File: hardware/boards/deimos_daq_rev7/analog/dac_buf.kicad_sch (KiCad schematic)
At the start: 4 parts, among them IC53001 INA826AIDR

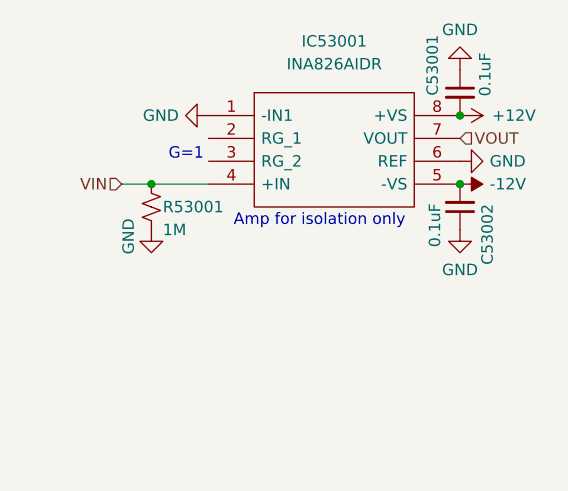
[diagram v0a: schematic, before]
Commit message: schematic updates for ovp rail and dac pulldown
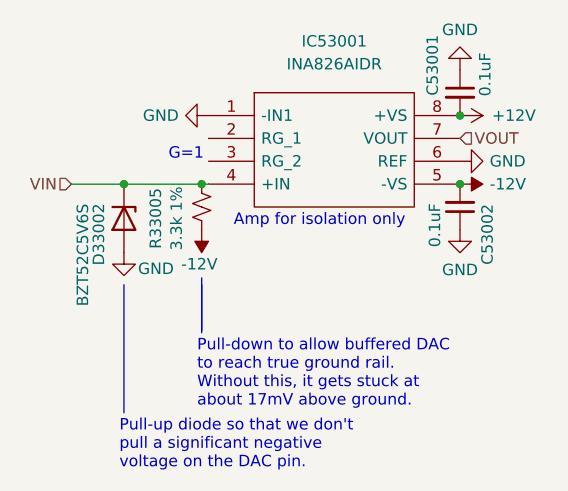
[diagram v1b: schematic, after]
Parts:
- removed R53001: 1M, Resistor_SMD:R_0402_1005Metric, symbol Device:R_Small_US
- added D33002: BZT52C5V6S, Diode_SMD:D_SOD-323, symbol Device:D_Zener
- added R33005: 3.3k 1%, Resistor_SMD:R_0402_1005Metric, symbol Device:R_Small_US
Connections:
- net -12V: now also R33005.1
- net GND: now also D33002.2 (A)
- net VIN: now also D33002.1 (K), R33005.2
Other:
- note added: "Pull-down to allow buffered DAC to reach true ground rail. Without this, it gets stuck at about 17mV above ground."
- note added: "Pull-up diode so that we don't pull a significant negative voltage on the DAC pin."

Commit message: wip to export more gpio pins
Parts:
- renumbered D33002 to D53001, R33005 to R53001
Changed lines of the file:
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@@
 		(on_board yes)
 		(dnp no)
-		(property "Reference" "R33005"
+		(property "Reference" "R53001"
 			(at 121.3866 109.728 90)
 			(effects
@@
 		)
 		(instances
+			(project "analog_i"
+				(path "/5a60c4b1-b6cb-416e-8883-8291fa089b87/c2baf18d-2b19-4edb-98b3-535275ee271f/13efaa5b-e400-45cc-91a0-978d4e7725f3"
+					(reference "R53001")
+					(unit 1)
+				)
+				(path "/5a60c4b1-b6cb-416e-8883-8291fa089b87/c2baf18d-2b19-4edb-98b3-535275ee271f/cebae258-d5b5-4a87-b6e3-430d71499c69"
+					(reference "R54001")
+					(unit 1)
+				)
+			)
 			(project "analog_frontend_panel"
 				(path "/c241d083-1323-4b4a-a540-956d0afb7b72/13efaa5b-e400-45cc-91a0-978d4e7725f3"
@@
 		(on_board yes)
 		(dnp no)
-		(property "Reference" "#PWR33002"
+		(property "Reference" "#PWR233"
 			(at 126.492 107.188 0)
 			(effects
@@
 		)
 		(instances
+			(project "analog_i"
+				(path "/5a60c4b1-b6cb-416e-8883-8291fa089b87/c2baf18d-2b19-4edb-98b3-535275ee271f/13efaa5b-e400-45cc-91a0-978d4e7725f3"
+					(reference "#PWR233")
+					(unit 1)
+				)
+				(path "/5a60c4b1-b6cb-416e-8883-8291fa089b87/c2baf18d-2b19-4edb-98b3-535275ee271f/cebae258-d5b5-4a87-b6e3-430d71499c69"
+					(reference "#PWR256")
+					(unit 1)
+				)
+			)
 			(project "analog_frontend_panel"
 				(path "/c241d083-1323-4b4a-a540-956d0afb7b72/13efaa5b-e400-45cc-91a0-978d4e7725f3"
@@
 		(on_board yes)
 		(dnp no)
-		(property "Reference" "#PWR33003"
+		(property "Reference" "#PWR217"
 			(at 117.856 119.888 0)
 			(effects
@@
 		)
 		(instances
+			(project "analog_i"
+				(path "/5a60c4b1-b6cb-416e-8883-8291fa089b87/c2baf18d-2b19-4edb-98b3-535275ee271f/13efaa5b-e400-45cc-91a0-978d4e7725f3"
+					(reference "#PWR217")
+					(unit 1)
+				)
+				(path "/5a60c4b1-b6cb-416e-8883-8291fa089b87/c2baf18d-2b19-4edb-98b3-535275ee271f/cebae258-d5b5-4a87-b6e3-430d71499c69"
+					(reference "#PWR245")
+					(unit 1)
+				)
+			)
 			(project "analog_frontend_panel"
 				(path "/c241d083-1323-4b4a-a540-956d0afb7b72/13efaa5b-e400-45cc-91a0-978d4e7725f3"
@@
 		(on_board yes)
 		(dnp no)
-		(property "Reference" "D33002"
+		(property "Reference" "D53001"
 			(at 115.062 111.506 0)
 			(effects
@@
 		)
 		(instances
+			(project "analog_i"
+				(path "/5a60c4b1-b6cb-416e-8883-8291fa089b87/c2baf18d-2b19-4edb-98b3-535275ee271f/13efaa5b-e400-45cc-91a0-978d4e7725f3"
+					(reference "D53001")
+					(unit 1)
+				)
+				(path "/5a60c4b1-b6cb-416e-8883-8291fa089b87/c2baf18d-2b19-4edb-98b3-535275ee271f/cebae258-d5b5-4a87-b6e3-430d71499c69"
+					(reference "D54001")
+					(unit 1)
+				)
+			)
 			(project "analog_frontend_panel"
 				(path "/c241d083-1323-4b4a-a540-956d0afb7b72/13efaa5b-e400-45cc-91a0-978d4e7725f3"
